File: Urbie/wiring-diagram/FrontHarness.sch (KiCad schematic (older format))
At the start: 19 parts

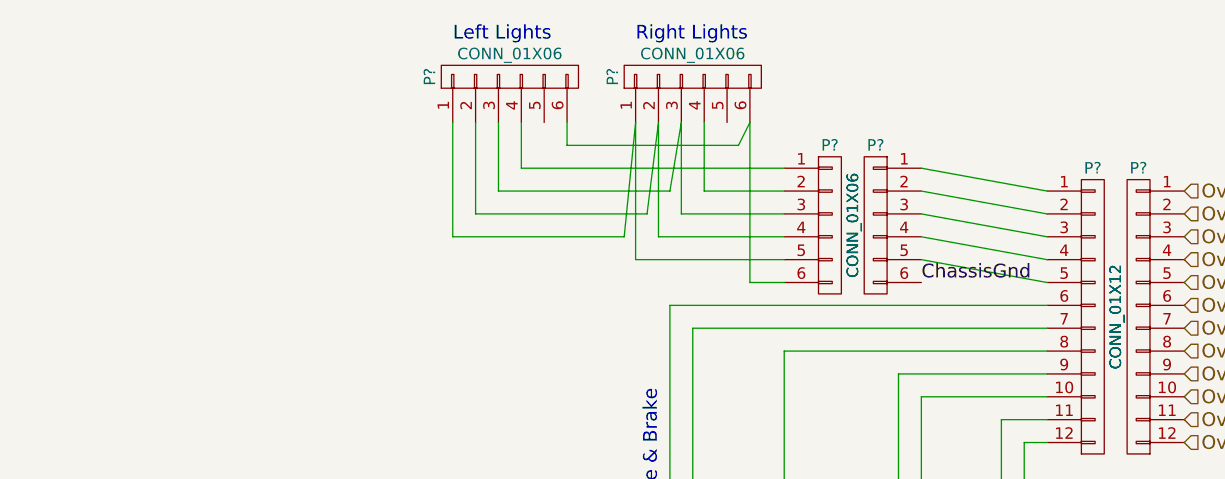
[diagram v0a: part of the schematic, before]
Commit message: Organizing relay box sheet
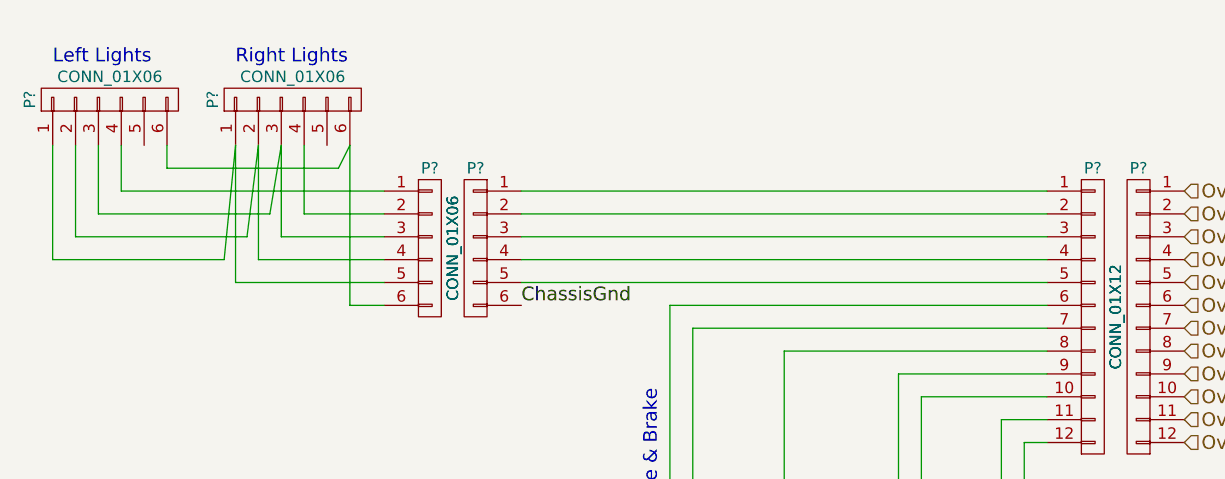
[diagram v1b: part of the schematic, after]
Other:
- moved on the sheet: P?
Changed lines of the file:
@@
 L CONN_01X06 P?
 U 1 1 5802823B
-P 8100 1600
-F 0 "P?" H 8100 1950 50  0000 C CNN
-F 1 "CONN_01X06" V 8200 1600 50  0000 C CNN
-F 2 "" H 8100 1600 50  0000 C CNN
-F 3 "" H 8100 1600 50  0000 C CNN
-	1    8100 1600
+P 6350 1700
+F 0 "P?" H 6350 2050 50  0000 C CNN
+F 1 "CONN_01X06" V 6450 1700 50  0000 C CNN
+F 2 "" H 6350 1700 50  0000 C CNN
+F 3 "" H 6350 1700 50  0000 C CNN
+	1    6350 1700
 	-1   0    0    -1
 $EndComp
@@
 L CONN_01X06 P?
 U 1 1 580282AA
-P 7900 1600
-F 0 "P?" H 7900 1950 50  0000 C CNN
-F 1 "CONN_01X06" V 8000 1600 50  0000 C CNN
-F 2 "" H 7900 1600 50  0000 C CNN
-F 3 "" H 7900 1600 50  0000 C CNN
-	1    7900 1600
+P 6150 1700
+F 0 "P?" H 6150 2050 50  0000 C CNN
+F 1 "CONN_01X06" V 6250 1700 50  0000 C CNN
+F 2 "" H 6150 1700 50  0000 C CNN
+F 3 "" H 6150 1700 50  0000 C CNN
+	1    6150 1700
 	1    0    0    -1
 $EndComp
@@
 L CONN_01X06 P?
 U 1 1 5802832D
-P 7300 950
-F 0 "P?" H 7300 1300 50  0000 C CNN
-F 1 "CONN_01X06" V 7400 950 50  0000 C CNN
-F 2 "" H 7300 950 50  0000 C CNN
-F 3 "" H 7300 950 50  0000 C CNN
-	1    7300 950
+P 5550 1050
+F 0 "P?" H 5550 1400 50  0000 C CNN
+F 1 "CONN_01X06" V 5650 1050 50  0000 C CNN
+F 2 "" H 5550 1050 50  0000 C CNN
+F 3 "" H 5550 1050 50  0000 C CNN
+	1    5550 1050
 	0    -1   -1   0
 $EndComp
@@
 L CONN_01X06 P?
 U 1 1 58028372
-P 6500 950
-F 0 "P?" H 6500 1300 50  0000 C CNN
-F 1 "CONN_01X06" V 6600 950 50  0000 C CNN
-F 2 "" H 6500 950 50  0000 C CNN
-F 3 "" H 6500 950 50  0000 C CNN
-	1    6500 950
-	0    -1   -1   0
-$EndComp
-Text Notes 7050 800  0    60   ~ 0
+P 4750 1050
+F 0 "P?" H 4750 1400 50  0000 C CNN
+F 1 "CONN_01X06" V 4850 1050 50  0000 C CNN
+F 2 "" H 4750 1050 50  0000 C CNN
+F 3 "" H 4750 1050 50  0000 C CNN
+	1    4750 1050
+	0    -1   -1   0
+$EndComp
+Text Notes 5300 900  0    60   ~ 0
 Right Lights
-Text Notes 6250 800  0    60   ~ 0
+Text Notes 4500 900  0    60   ~ 0
 Left Lights
 Wire Wire Line
-	7700 1350 6550 1350
-Wire Wire Line
-	6550 1350 6550 1150
-Wire Wire Line
-	7700 1450 7350 1450
-Wire Wire Line
-	7350 1450 7350 1150
-Wire Wire Line
-	7550 1850 7700 1850
-Wire Wire Line
-	7500 1250 6750 1250
-Wire Wire Line
-	6750 1250 6750 1150
-Wire Wire Line
-	7500 1250 7550 1150
-Wire Wire Line
-	7550 1150 7550 1850
-Wire Wire Line
-	7250 1150 7200 1450
-Wire Wire Line
-	7200 1450 6450 1450
-Wire Wire Line
-	6450 1450 6450 1150
-Wire Wire Line
-	7700 1550 7250 1550
-Wire Wire Line
-	7250 1550 7250 1150
-Wire Wire Line
-	7150 1150 7100 1550
-Wire Wire Line
-	7100 1550 6350 1550
-Wire Wire Line
-	6350 1550 6350 1150
-Wire Wire Line
-	7700 1650 7150 1650
-Wire Wire Line
-	7150 1650 7150 1150
-Wire Wire Line
-	7050 1150 7000 1650
-Wire Wire Line
-	7000 1650 6250 1650
-Wire Wire Line
-	6250 1650 6250 1150
-Wire Wire Line
-	7700 1750 7050 1750
-Wire Wire Line
-	7050 1750 7050 1150
-Wire Wire Line
-	8300 1350 8850 1450
-Wire Wire Line
-	8300 1450 8850 1550
-Wire Wire Line
-	8300 1550 8850 1650
-Wire Wire Line
-	8300 1650 8850 1750
-Wire Wire Line
-	8300 1750 8850 1850
+	5950 1450 4800 1450
+Wire Wire Line
+	4800 1450 4800 1250
+Wire Wire Line
+	5950 1550 5600 1550
+Wire Wire Line
+	5600 1550 5600 1250
+Wire Wire Line
+	5800 1950 5950 1950
+Wire Wire Line
+	5750 1350 5000 1350
+Wire Wire Line
+	5000 1350 5000 1250
+Wire Wire Line
+	5750 1350 5800 1250
+Wire Wire Line
+	5800 1250 5800 1950
+Wire Wire Line
+	5500 1250 5450 1550
+Wire Wire Line
+	5450 1550 4700 1550
+Wire Wire Line
+	4700 1550 4700 1250
+Wire Wire Line
+	5950 1650 5500 1650
+Wire Wire Line
+	5500 1650 5500 1250
+Wire Wire Line
+	5400 1250 5350 1650
+Wire Wire Line
+	5350 1650 4600 1650
+Wire Wire Line
+	4600 1650 4600 1250
+Wire Wire Line
+	5950 1750 5400 1750
+Wire Wire Line
+	5400 1750 5400 1250
+Wire Wire Line
+	5300 1250 5250 1750
+Wire Wire Line
+	5250 1750 4500 1750
+Wire Wire Line
+	4500 1750 4500 1250
+Wire Wire Line
+	5950 1850 5300 1850
+Wire Wire Line
+	5300 1850 5300 1250
 $Comp
 L CONN_01X02 P?
@@
 Wire Wire Line
 	8200 2250 8850 2250
-Text Label 8300 1850 0    60   ~ 0
+Text Label 6550 1950 0    60   ~ 0
 ChassisGnd
 Wire Wire Line
@@
 Wire Wire Line
 	8750 4850 8750 4600
+Wire Wire Line
+	6550 1450 8850 1450
+Wire Wire Line
+	6550 1550 8850 1550
+Wire Wire Line
+	6550 1650 8850 1650
+Wire Wire Line
+	6550 1750 8850 1750
+Wire Wire Line
+	6550 1850 8850 1850
 $EndSCHEMATC

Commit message: fixed some stuff
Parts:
- removed CR?: CR, symbol CR
- added M?: Motor, symbol Motor
- P?: value CONN_01X06 -> Front Lights
- P?: value CONN_01X06 -> Right Lights
- P?: value CONN_01X06 -> Left Lights
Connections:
- net ChassisGnd: now also M?.2
- net at P?.1 (P1): now also M?.1; no longer P?.2 (P2)
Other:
- note removed: "Left Lights"
- note removed: "Right Lights"
- moved on the sheet: P?, SP?, SW?

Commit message: updated 1593BB-box footprint
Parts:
- removed P? (x2): CONN_01X12, symbol CONN_01X12
- removed P? (x4): CONN_01X02, symbol CONN_01X02
- removed SW?: SW_NO, symbol SW_NO
- added P? (x2): CONN_01X15, symbol CONN_01X15
- added P? (x4): CONN_01X04, symbol CONN_01X04
- added U?: Throttle, symbol Throttle
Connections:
- net ChassisGnd: no longer P?.2 (P2), P?.6 (P6)
- net Ov10WiperPwr: now also P?.10 (P10)
- net Ov11AcceleratorYellow: now also P?.11 (P11)
- net Ov12AcceleratorRed: now also P?.12 (P12)
- net Ov1LftBlnk: now also P?.1 (P1)
- net Ov2RtBlnk: now also P?.2 (P2)
- net Ov3: now also P?.3 (P3)
- net Ov4: now also P?.4 (P4)
- net Ov5: now also P?.5 (P5)
- net Ov6Brake1: now also P?.6 (P6)
- net Ov7BBrake2: now also P?.7 (P7)
- net Ov8Horn: now also P?.8 (P8)
- net Ov9WiperPwr: now also P?.9 (P9)
- net at P?.1 (P1): now also P?.1 (P1)
- net at P?.2 (P2): now also P?.2 (P2)
- net at P?.3 (P3): now also P?.3 (P3)
- net at P?.4 (P4): now also P?.4 (P4)
- net at P?.5 (P5): now also P?.5 (P5)
- net at P?.1 (P1): now also P?.6 (P6)
- net at P?.2 (P2): now also P?.7 (P7)
- net Brn: now reaches P?.1 (P1)
- net Brn: now also P?.8 (P8)
- new net: P?.4 (P4), U?.blk (GND)
- new net: P?.2 (P2), U?.grn (sig)
- new net: P?.1 (P1), U?.red (5v)
- new net Blk: P?.13 (P13), P?.14 (P14), P?.15 (P15), P?.2 (P2), P?.4 (P4), P?.4 (P4), P?.6 (P6)
- new net Orng: P?.1 (P1), P?.9 (P9)
- new net Ov13:GND: P?.13 (P13)
- new net Ov14:GND: P?.14 (P14)
- new net Ov15:GND: P?.15 (P15)
- new net Red: P?.1 (P1), P?.12 (P12)
- new net White: P?.10 (P10), P?.3 (P3)
- new net Yel: P?.11 (P11), P?.2 (P2)
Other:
- moved on the sheet: P?, SW?
